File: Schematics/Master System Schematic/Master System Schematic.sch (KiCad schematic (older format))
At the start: 40 parts, among them J1 GND, J10 +12V, J11 Charger +12V, J2 TS+, J3 TS-, J8 Charger GND, K12 Cooling Pump Relay, M1 Cooling Pump, SW1 GLVMS, SW10 SMD, SW11 BRAKE_SWITCH, SW12 SW_SPST_Pressure, SW13 SW_SPST_Pressure, SW2 SideMounted (BRB), SW3 SideMounted (BRB), SW4 Brake Over-Travel Switch, SW5 Latching Circuit Reset, SW6 Cockpit Shutdown (BRB), SW7 TSMS, SW8 SMD, SW9 HVD, U3 FuseBox_PSZACCEPS052H, U4 Bender_Isometer_IR155-3204, U6 RinehartPM100DX_MotorControll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, U7 Emrax228HV_Motor

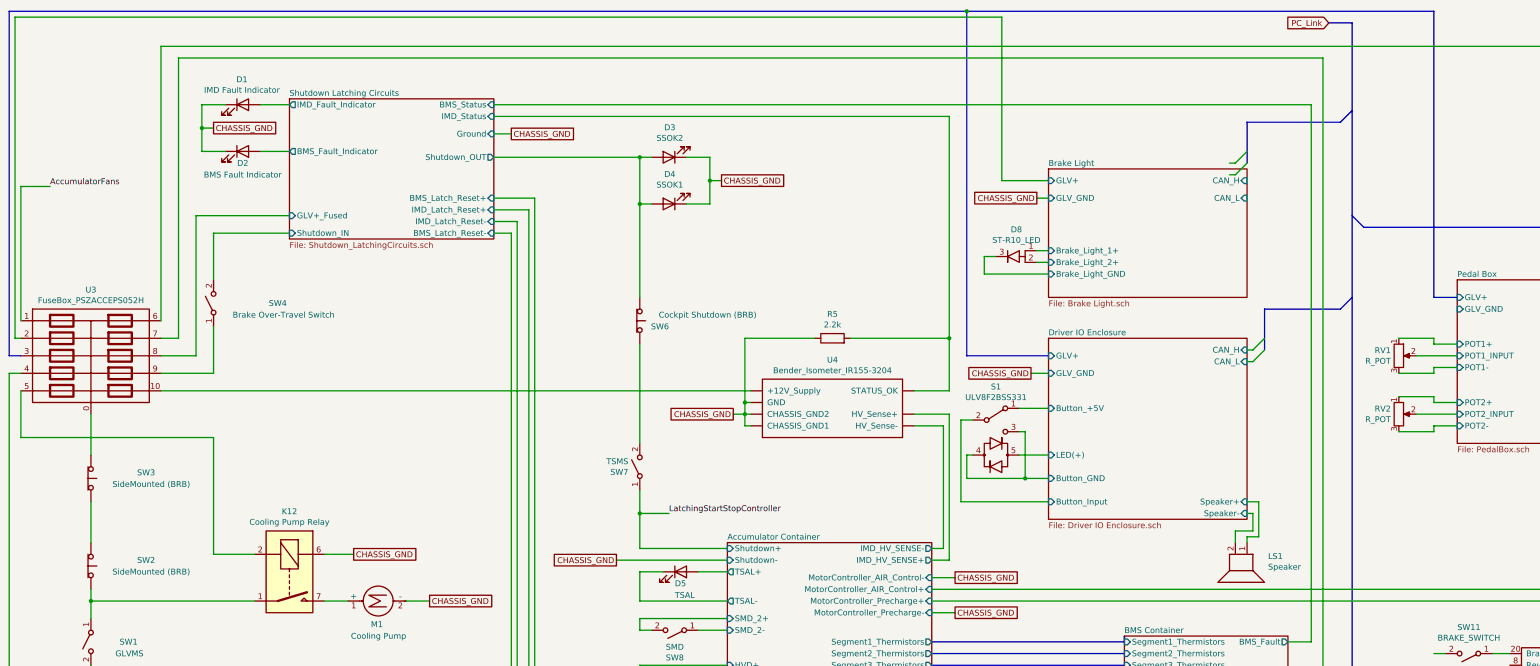
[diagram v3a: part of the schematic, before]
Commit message: Started Voltage tap pcbs
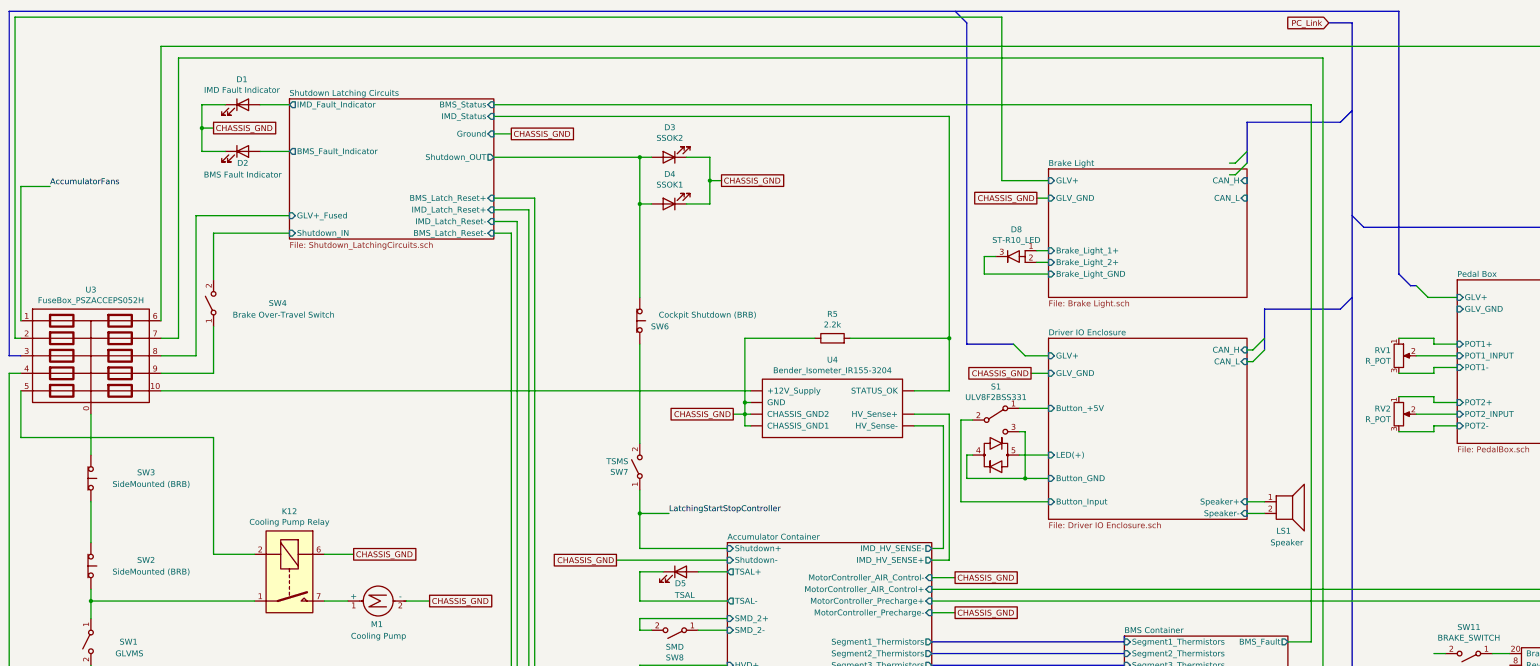
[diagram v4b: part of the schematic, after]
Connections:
- new net: U3.6, U6.23 (CANB_H), U6.8 (Reverse_Enable_Switch)
- new net: U6.~ (TS-), U7.~ (AC3) (x2)
- now unconnected: U6.23 (CANB_H), U6.8 (Reverse_Enable_Switch)
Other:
- moved on the sheet: LS1
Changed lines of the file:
@@
 $Descr B 17000 11000
 encoding utf-8
-Sheet 1 13
+Sheet 1 17
 Title "NER FH 2020-2021 Master Electrical Schematic"
 Date "2020-10-12"
@@
 L Device:Speaker LS1
 U 1 1 5F9B2999
-P 11150 5450
-F 0 "LS1" V 11067 5630 50  0000 L CNN
-F 1 "Speaker" V 11158 5630 50  0000 L CNN
-F 2 "" H 11150 5250 50  0001 C CNN
-F 3 "~" H 11140 5400 50  0001 C CNN
-	1    11150 5450
-	0    1    1    0
-$EndComp
-Wire Wire Line
-	11150 5000 11200 5000
-Wire Wire Line
-	11200 5000 11200 5150
-Wire Wire Line
-	11200 5150 11050 5150
-Wire Wire Line
-	11050 5150 11050 5250
-Wire Wire Line
-	11150 4900 11250 4900
-Wire Wire Line
-	11250 4900 11250 5200
-Wire Wire Line
-	11250 5200 11150 5200
-Wire Wire Line
-	11150 5200 11150 5250
+P 11500 4900
+F 0 "LS1" H 11400 4650 50  0000 L CNN
+F 1 "Speaker" H 11350 4550 50  0000 L CNN
+F 2 "" H 11500 4700 50  0001 C CNN
+F 3 "~" H 11490 4850 50  0001 C CNN
+	1    11500 4900
+	1    0    0    -1
+$EndComp
 Wire Wire Line
 	8650 8150 13400 8150
@@
 	600  750  9050 750
 Wire Bus Line
-	9450 3650 8750 3650
-Wire Bus Line
-	8750 3650 8750 700
-Connection ~ 8750 700
-Wire Bus Line
-	12950 3150 12750 3150
-Wire Bus Line
-	12750 3150 12750 700
-Wire Bus Line
-	8750 700  12750 700
-Wire Bus Line
 	550  3650 650  3650
 Wire Bus Line
 	550  700  550  3650
-Wire Bus Line
-	550  700  8750 700
 Wire Wire Line
 	650  3500 600  3500
@@
 Wire Wire Line
 	10000 7300 10100 7300
+Entry Bus Bus
+	8650 700  8750 800
+Entry Wire Line
+	9150 3550 9250 3650
+Wire Wire Line
+	9250 3650 9450 3650
+Wire Bus Line
+	12450 2950 12450 700
+Entry Bus Bus
+	12450 2950 12550 3050
+Wire Bus Line
+	12550 3050 12600 3050
+Entry Wire Line
+	12600 3050 12700 3150
+Wire Wire Line
+	12700 3150 12950 3150
+Wire Bus Line
+	9150 3550 8750 3550
+Wire Bus Line
+	8750 800  8750 3550
+Wire Wire Line
+	11150 5000 11300 5000
+Wire Wire Line
+	11150 4900 11300 4900
+Wire Bus Line
+	550  700  12450 700
 Wire Bus Line
 	11300 3250 11300 3600

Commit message: Fixed Broken Library References
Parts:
- K12: symbol Master-System-Schematic-cache:Relay_DIPxx-1Axx-11x -> Relay:DIPxx-1Axx-11x
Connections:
- new net: U3.6, U6.23 (CANB_H), U6.8 (Reverse_Enable_Switch)
- new net: U6.~ (TS-), U7.~ (AC3) (x2)
- now unconnected: U6.23 (CANB_H), U6.8 (Reverse_Enable_Switch)
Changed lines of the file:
@@
 EESchema Schematic File Version 4
+LIBS:Master System Schematic-cache
 EELAYER 30 0
 EELAYER END
@@
 	1250 5750 1250 5900
 $Comp
-L Master-System-Schematic-cache:Relay_DIPxx-1Axx-11x K12
+L Relay:DIPxx-1Axx-11x K12
 U 1 1 5F9B5A7A
 P 2950 5550

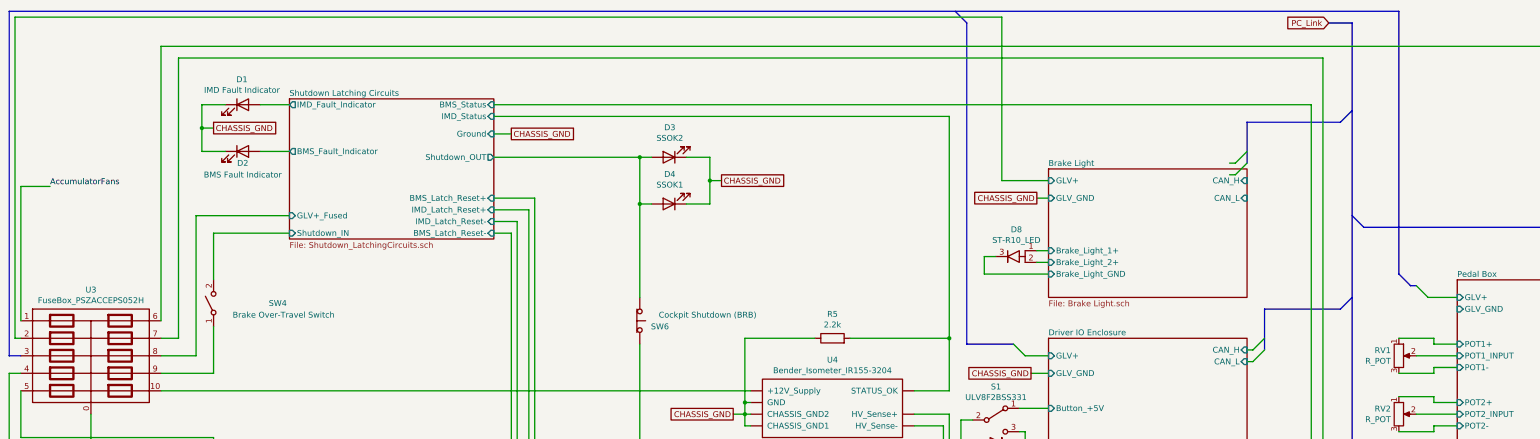
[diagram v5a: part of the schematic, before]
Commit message: Clean up for merge
>cleaned wire runs on top sheet
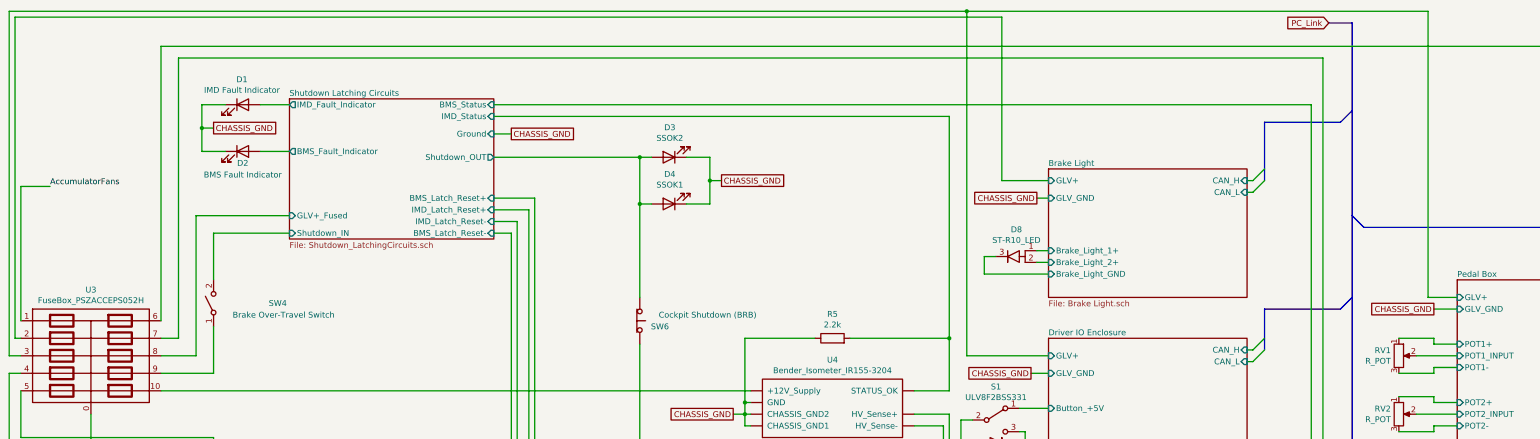
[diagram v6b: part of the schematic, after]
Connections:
- net Driver IO Enclosure/GLV+: now also U3.3
- new net: U3.6, U6.23 (CANB_H), U6.8 (Reverse_Enable_Switch)
- new net: U6.~ (TS-), U7.~ (AC3) (x2)
- now unconnected: U6.23 (CANB_H), U6.8 (Reverse_Enable_Switch)
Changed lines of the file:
@@
 EESchema Schematic File Version 4
-LIBS:Master System Schematic-cache
 EELAYER 30 0
 EELAYER END
@@
 Wire Wire Line
 	5950 5300 6700 5300
-$Sheet
-S 9450 2050 1700 1100
-U 5F890A03
-F0 "Brake Light" 50
-F1 "Brake Light.sch" 50
-F2 "CAN_H" I R 11150 2150 50
-F3 "CAN_L" I R 11150 2300 50
-F4 "GLV+" I L 9450 2150 50
-F5 "GLV_GND" I L 9450 2300 50
-F6 "Brake_Light_1+" I L 9450 2750 50
-F7 "Brake_Light_2+" I L 9450 2850 50
-F8 "Brake_Light_GND" I L 9450 2950 50
-$EndSheet
 $Comp
 L NER:ULV8F2BSS331 S1
@@
 	12050 800  11850 800
 Wire Wire Line
-	11000 2000 11050 2000
-Wire Wire Line
-	11000 2100 11050 2100
-Entry Wire Line
-	11050 2100 11150 2000
-Entry Wire Line
-	11050 2000 11150 1900
-Wire Wire Line
 	14400 3150 14450 3150
 Wire Wire Line
@@
 Wire Bus Line
 	12150 2550 14550 2550
-Wire Bus Line
-	11150 1650 11950 1650
 Wire Wire Line
 	11150 3600 11200 3600
@@
 Wire Wire Line
 	600  750  9050 750
-Wire Bus Line
-	550  3650 650  3650
-Wire Bus Line
-	550  700  550  3650
 Wire Wire Line
 	650  3500 600  3500
@@
 Wire Wire Line
 	10000 7300 10100 7300
-Entry Bus Bus
-	8650 700  8750 800
+Wire Wire Line
+	11150 5000 11300 5000
+Wire Wire Line
+	11150 4900 11300 4900
+Wire Wire Line
+	650  3650 550  3650
+Wire Wire Line
+	550  3650 550  700
+Wire Wire Line
+	550  700  8750 700
+Wire Wire Line
+	9450 3650 8750 3650
+Wire Wire Line
+	8750 3650 8750 700
+Connection ~ 8750 700
+Wire Wire Line
+	11150 2250 11200 2250
 Entry Wire Line
-	9150 3550 9250 3650
-Wire Wire Line
-	9250 3650 9450 3650
-Wire Bus Line
-	12450 2950 12450 700
-Entry Bus Bus
-	12450 2950 12550 3050
-Wire Bus Line
-	12550 3050 12600 3050
+	11200 2250 11300 2150
+Wire Wire Line
+	11150 2150 11200 2150
+$Sheet
+S 9450 2050 1700 1100
+U 5F890A03
+F0 "Brake Light" 50
+F1 "Brake Light.sch" 50
+F2 "CAN_H" I R 11150 2150 50
+F3 "CAN_L" I R 11150 2250 50
+F4 "GLV+" I L 9450 2150 50
+F5 "GLV_GND" I L 9450 2300 50
+F6 "Brake_Light_1+" I L 9450 2750 50
+F7 "Brake_Light_2+" I L 9450 2850 50
+F8 "Brake_Light_GND" I L 9450 2950 50
+$EndSheet
 Entry Wire Line
-	12600 3050 12700 3150
+	11200 2150 11300 2050
 Wire Wire Line
 	12700 3150 12950 3150
 Wire Bus Line
-	9150 3550 8750 3550
-Wire Bus Line
-	8750 800  8750 3550
-Wire Wire Line
-	11150 5000 11300 5000
-Wire Wire Line
-	11150 4900 11300 4900
-Wire Bus Line
-	550  700  12450 700
+	11300 1650 11950 1650
+Wire Wire Line
+	12700 3150 12700 700
+Wire Wire Line
+	8750 700  12700 700
+Text GLabel 12750 3250 0    50   UnSpc ~ 0
+CHASSIS_GND
+Wire Wire Line
+	12750 3250 12950 3250
 Wire Bus Line
 	11300 3250 11300 3600
@@
 	14550 2550 14550 3150
 Wire Bus Line
-	11150 1650 11150 2000
+	11300 1650 11300 2150
 Wire Bus Line
 	12050 800  12050 6750

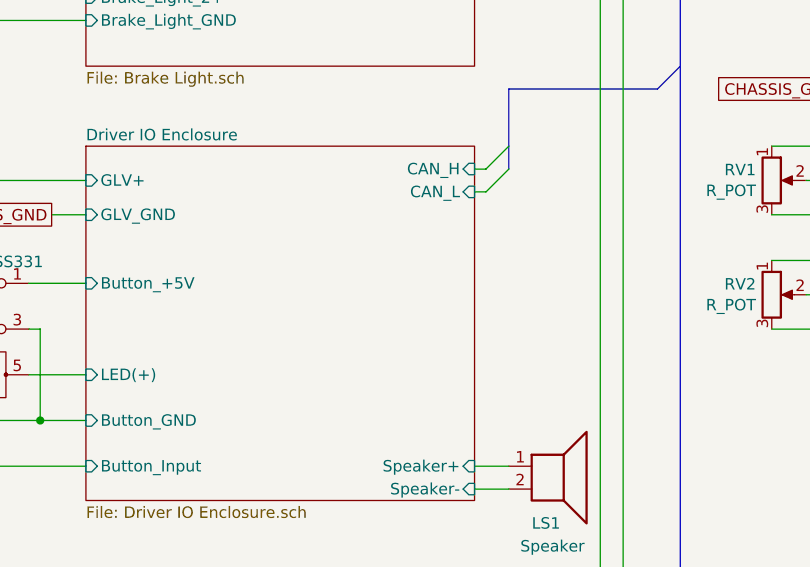
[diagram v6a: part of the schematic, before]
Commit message: StartEnable w/ Voltage Divider
Added StartEnable wire to the dashboard can box and added a voltage divider with proper resistors to bring voltage down from 12V to 5V.
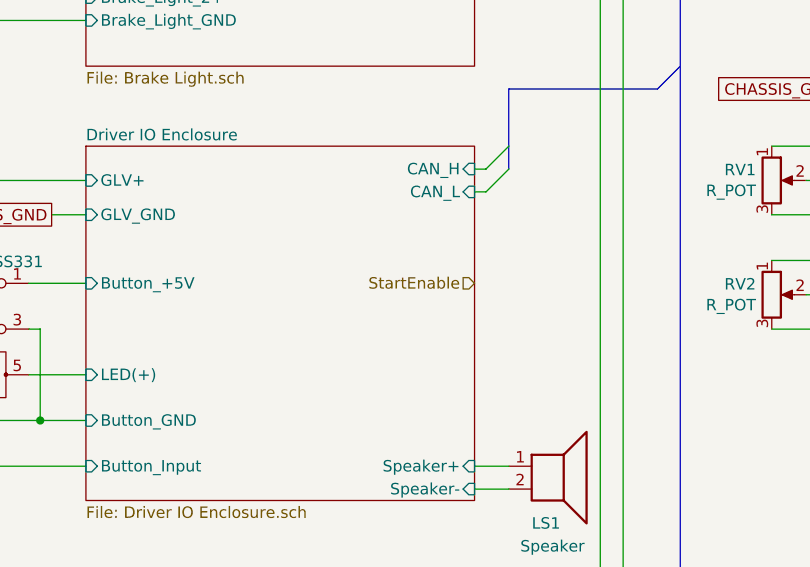
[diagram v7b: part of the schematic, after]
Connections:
- new net: U3.6, U6.23 (CANB_H), U6.8 (Reverse_Enable_Switch)
- new net: U6.~ (TS-), U7.~ (AC3) (x2)
- now unconnected: U6.23 (CANB_H), U6.8 (Reverse_Enable_Switch)
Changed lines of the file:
@@
 	15200 7250 15200 7500
 Connection ~ 15200 7500
-$Sheet
-S 9450 3500 1700 1550
-U 5F647A32
-F0 "Driver IO Enclosure" 50
-F1 "Driver IO Enclosure.sch" 50
-F2 "CAN_L" I R 11150 3700 50
-F3 "CAN_H" I R 11150 3600 50
-F4 "GLV+" I L 9450 3650 50
-F5 "GLV_GND" I L 9450 3800 50
-F6 "LED(+)" I L 9450 4500 50
-F7 "Button_GND" I L 9450 4700 50
-F8 "Button_Input" I L 9450 4900 50
-F9 "Button_+5V" I L 9450 4100 50
-F10 "Speaker+" I R 11150 4900 50
-F11 "Speaker-" I R 11150 5000 50
-$EndSheet
 Text GLabel 15200 7250 1    50   UnSpc ~ 0
 CHASSIS_GND
@@
 Wire Wire Line
 	12750 3250 12950 3250
+$Sheet
+S 9450 3500 1700 1550
+U 5F647A32
+F0 "Driver IO Enclosure" 50
+F1 "Driver IO Enclosure.sch" 50
+F2 "CAN_L" I R 11150 3700 50
+F3 "CAN_H" I R 11150 3600 50
+F4 "GLV+" I L 9450 3650 50
+F5 "GLV_GND" I L 9450 3800 50
+F6 "LED(+)" I L 9450 4500 50
+F7 "Button_GND" I L 9450 4700 50
+F8 "Button_Input" I L 9450 4900 50
+F9 "Button_+5V" I L 9450 4100 50
+F10 "Speaker+" I R 11150 4900 50
+F11 "Speaker-" I R 11150 5000 50
+$EndSheet
+Wire Bus Line
+	11300 1650 11300 2150
 Wire Bus Line
 	11300 3250 11300 3600
@@
 	14550 2550 14550 3150
 Wire Bus Line
-	11300 1650 11300 2150
-Wire Bus Line
 	12050 800  12050 6750
+Text HLabel 11150 4100 0    50   Input ~ 0
+StartEnable
 $EndSCHEMATC

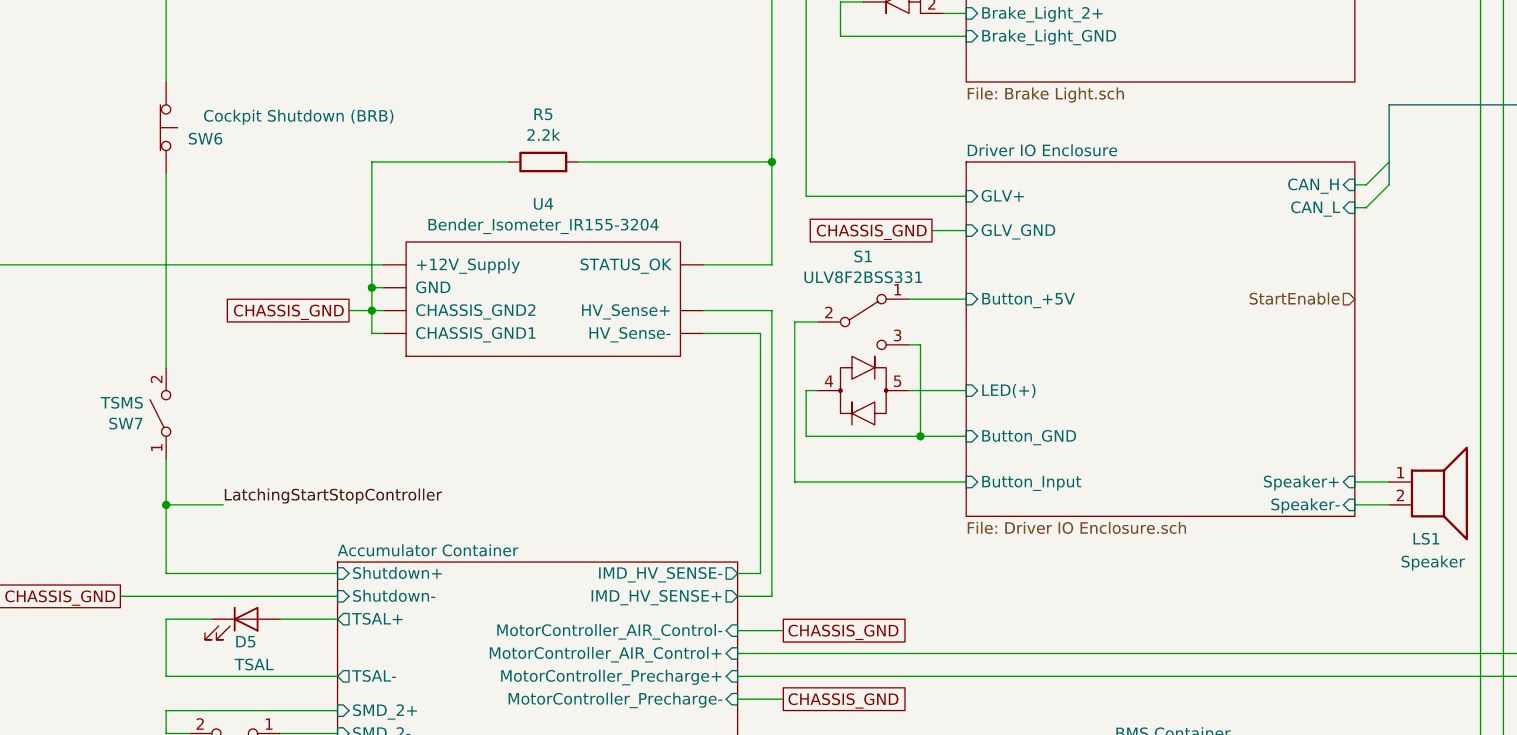
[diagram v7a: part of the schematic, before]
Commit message: Fixed Pin and Updated Title Block
-Fixed incorrectly imported pin
-Actually wired the pin in the master schematic
-Updated title block
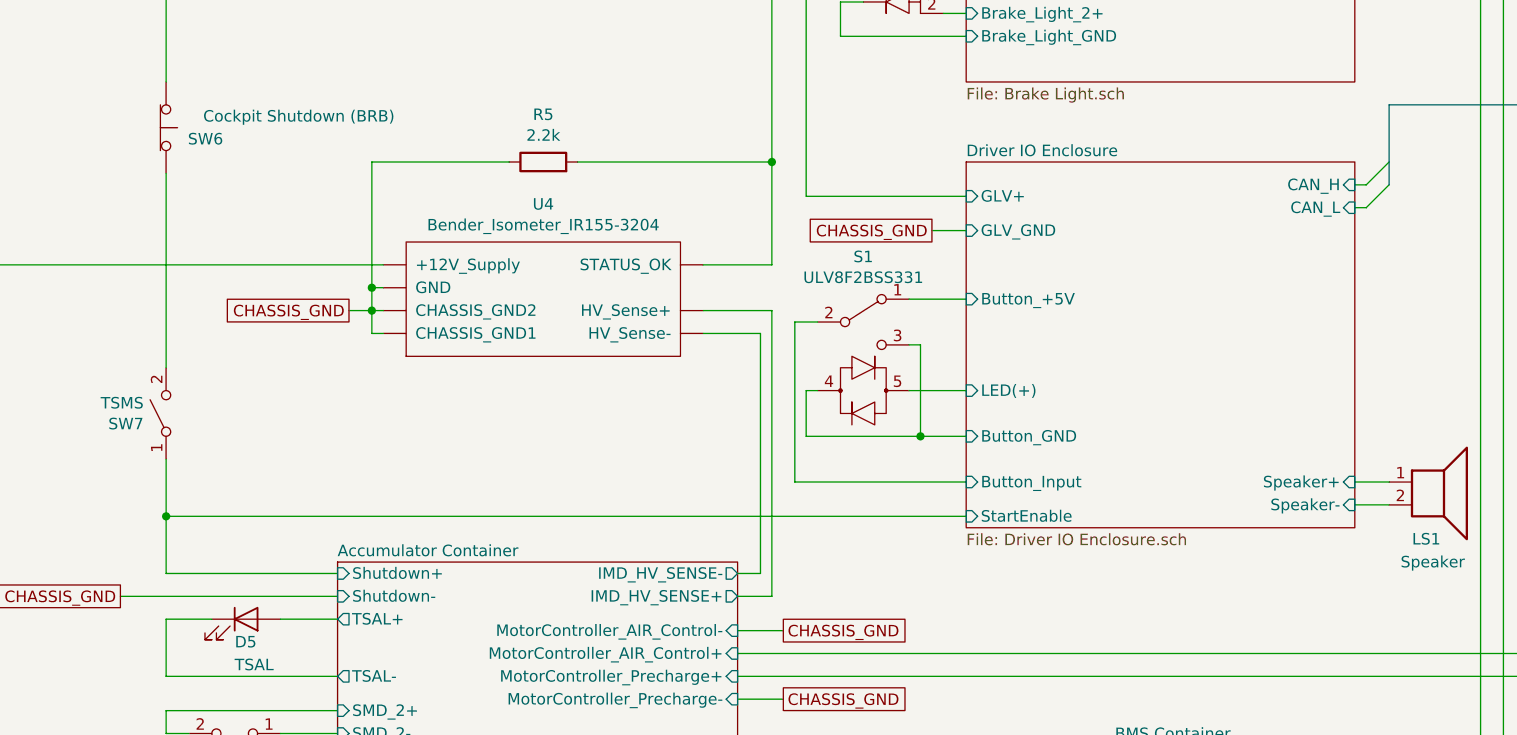
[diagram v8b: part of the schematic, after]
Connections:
- net LatchingStartStopController renamed Accumulator Container/Shutdown+
- new net: U3.6, U6.23 (CANB_H), U6.8 (Reverse_Enable_Switch)
- new net: U6.~ (TS-), U7.~ (AC3) (x2)
- now unconnected: U6.23 (CANB_H), U6.8 (Reverse_Enable_Switch)
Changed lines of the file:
@@
 EESchema Schematic File Version 4
+LIBS:Master System Schematic-cache
 EELAYER 30 0
 EELAYER END
@@
 Sheet 1 17
 Title "NER FH 2020-2021 Master Electrical Schematic"
-Date "2020-10-12"
-Rev "3"
+Date "2020-10-15"
+Rev "4"
 Comp "Northeastern Electric Racing"
 Comment1 "Dylan Gardner, Matthew McCauley"
@@
 Text GLabel 1400 7900 2    50   UnSpc ~ 0
 CHASSIS_GND
-Text Label 6200 5000 0    50   ~ 0
-LatchingStartStopController
 Text GLabel 6650 2150 2    50   UnSpc ~ 0
 CHASSIS_GND
@@
 Wire Wire Line
 	1250 4900 1250 5250
-Wire Wire Line
-	6200 5000 5950 5000
 $Comp
 L Connector:Conn_01x01_Female J3
@@
 	12750 4250 12950 4250
 Wire Wire Line
-	5950 4800 5950 5000
-Wire Wire Line
 	8600 5400 8600 4150
 Wire Wire Line
@@
 	5950 1950 4700 1950
 Connection ~ 5950 1950
-Connection ~ 5950 5000
-Wire Wire Line
-	5950 5000 5950 5300
 Wire Wire Line
 	5950 5300 6700 5300
@@
 	12750 3250 12950 3250
 $Sheet
-S 9450 3500 1700 1550
+S 9450 3500 1700 1600
 U 5F647A32
 F0 "Driver IO Enclosure" 50
@@
 F10 "Speaker+" I R 11150 4900 50
 F11 "Speaker-" I R 11150 5000 50
+F12 "StartEnable" I L 9450 5050 50
 $EndSheet
+Wire Wire Line
+	5950 4800 5950 5050
+Wire Wire Line
+	9450 5050 5950 5050
 Wire Bus Line
 	11300 1650 11300 2150
@@
 Wire Bus Line
 	12050 800  12050 6750
-Text HLabel 11150 4100 0    50   Input ~ 0
-StartEnable
+Connection ~ 5950 5050
+Wire Wire Line
+	5950 5050 5950 5300
 $EndSCHEMATC
